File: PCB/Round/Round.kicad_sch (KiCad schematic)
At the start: 59 parts, among them J3 Conn, SW1 ESE13V01D, U1 PN532, U2 QR, Y1 27.12MHz

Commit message: Images
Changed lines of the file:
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@@
 (kicad_sch
-	(version 20231120)
+	(version 20241209)
 	(generator "eeschema")
-	(generator_version "8.0")
+	(generator_version "9.0")
 	(paper "A4")
 	(title_block
@@
 		(comment 1 "www.me.uk")
 	)
+	(text "GND\nVCC\nTX\nRX\nBell"
+		(exclude_from_sim no)
+		(at 241.935 62.865 0)
+		(effects
+			(font
+				(size 1.27 1.27)
+			)
+			(justify left bottom)
+		)
+	)
 	(junction
 		(at 85.09 113.03)
@@
 		)
 	)
-	(text "GND\nVCC\nTX\nRX\nBell"
-		(exclude_from_sim no)
-		(at 241.935 62.865 0)
-		(effects
-			(font
-				(size 1.27 1.27)
-			)
-			(justify left bottom)
-		)
-	)
 	(symbol
 		(lib_id "RevK:PN532-Antenna")
@@
 		)
 	)
+	(embedded_fonts no)
 )

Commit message: PCB Update
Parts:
- D1: LCSC Part # C157737 -> (none); MPN (none) -> C157737
- D10, D4, D5, D6, D7, D8, D9: LCSC Part # C5137770 -> (none); MPN (none) -> C5137770
- D2: LCSC Part # C125108 -> (none); MPN (none) -> C125108
- D3: LCSC Part # C125107 -> (none); MPN (none) -> C125107
- J3: JLCPCB Rotation Offset 90 -> (none); LCSC Part # C780063 -> (none); MPN (none) -> C780063
- L1, L2: LCSC Part # C75639 -> (none); MPN (none) -> C75639
- R4: LCSC Part # C114612 -> (none); MPN (none) -> C114612
- R5: LCSC Part # C22548 -> (none); MPN (none) -> C22548
- U1: JLCPCB Rotation Offset -90 -> (none)
- Y1: JLCPCB Rotation Offset 180 -> (none); LCSC Part # C70591 -> (none); MPN (none) -> C70591
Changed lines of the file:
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@@
 			)
 		)
-		(property "JLCPCB Rotation Offset" "-90"
-			(at 163.83 139.7 0)
-			(effects
-				(font
-					(size 1.27 1.27)
-				)
-				(hide yes)
-			)
-		)
 		(pin "1"
 		)
@@
 			)
 		)
-		(property "LCSC Part #" "C75639"
+		(property "MPN" "C75639"
 			(at 99.06 92.71 90)
 			(effects
@@
 			)
 		)
-		(property "LCSC Part #" "C75639"
+		(property "MPN" "C75639"
 			(at 99.06 113.03 90)
 			(effects
@@
 			)
 		)
-		(property "LCSC Part #" "C70591"
-			(at 158.75 144.78 0)
-			(effects
-				(font
-					(size 1.27 1.27)
-				)
-				(hide yes)
-			)
-		)
-		(property "JLCPCB Rotation Offset" "180"
+		(property "MPN" "C70591"
 			(at 158.75 144.78 0)
 			(effects
@@
 			)
 		)
-		(property "LCSC Part #" "C114612"
+		(property "MPN" "C114612"
 			(at 101.6 127 90)
 			(effects
@@
 			)
 		)
-		(property "LCSC Part #" "C22548"
+		(property "MPN" "C22548"
 			(at 128.27 123.19 0)
 			(effects
@@
 			)
 		)
-		(property "LCSC Part #" "C780063"
-			(at 247.65 57.785 0)
-			(effects
-				(font
-					(size 1.27 1.27)
-				)
-				(hide yes)
-			)
-		)
-		(property "JLCPCB Rotation Offset" "90"
+		(property "MPN" "C780063"
 			(at 247.65 57.785 0)
 			(effects
@@
 			)
 		)
-		(property "LCSC Part #" "C157737"
+		(property "MPN" "C157737"
 			(at 199.39 30.48 0)
 			(effects
@@
 			)
 		)
-		(property "LCSC Part #" "C125108"
+		(property "MPN" "C125108"
 			(at 199.39 45.72 0)
 			(effects
@@
 			)
 		)
-		(property "LCSC Part #" "C125107"
+		(property "MPN" "C125107"
 			(at 199.39 62.23 0)
 			(effects
@@
 			)
 		)
-		(property "LCSC Part #" "C5137770"
+		(property "MPN" "C5137770"
 			(at 257.175 113.03 0)
 			(effects
@@
 			)
 		)
-		(property "LCSC Part #" "C5137770"
+		(property "MPN" "C5137770"
 			(at 257.175 123.19 0)
 			(effects
@@
 			)
 		)
-		(property "LCSC Part #" "C5137770"
+		(property "MPN" "C5137770"
 			(at 257.175 139.7 0)
 			(effects
@@
 			)
 		)
-		(property "LCSC Part #" "C5137770"
+		(property "MPN" "C5137770"
 			(at 199.39 71.12 0)
 			(effects
@@
 			)
 		)
-		(property "LCSC Part #" "C5137770"
+		(property "MPN" "C5137770"
 			(at 267.97 51.435 0)
 			(effects
@@
 			)
 		)
-		(property "LCSC Part #" "C5137770"
+		(property "MPN" "C5137770"
 			(at 199.39 54.61 0)
 			(effects
@@
 			)
 		)
-		(property "LCSC Part #" "C5137770"
+		(property "MPN" "C5137770"
 			(at 199.39 39.37 0)
 			(effects

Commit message: Tidy
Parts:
- removed U2: QR, RevK:QR-PN532, symbol RevK:QR
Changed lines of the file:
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@@
 (kicad_sch
-	(version 20241209)
+	(version 20250114)
 	(generator "eeschema")
 	(generator_version "9.0")
@@
 		(dnp no)
 		(property "Reference" "R4"
-			(at 101.6 132.08 90)
+			(at 101.854 129.54 90)
 			(effects
 				(font
@@
 		)
 		(property "Value" "2k7 1%"
-			(at 101.6 124.0536 90)
+			(at 103.632 127 90)
 			(effects
 				(font
@@
 		(dnp no)
 		(property "Reference" "R6"
-			(at 151.13 31.5722 90)
+			(at 151.13 34.544 90)
 			(effects
 				(font
@@
 		)
 		(property "Value" "10K"
-			(at 151.13 33.8836 90)
+			(at 151.13 36.83 90)
 			(effects
 				(font
@@
 		(dnp no)
 		(property "Reference" "R8"
-			(at 213.36 25.2222 90)
+			(at 213.36 28.448 90)
 			(effects
 				(font
@@
 		)
 		(property "Value" "100R"
-			(at 213.36 27.5336 90)
+			(at 213.36 30.48 90)
 			(effects
 				(font
@@
 		(dnp no)
 		(property "Reference" "R9"
-			(at 213.36 40.4622 90)
+			(at 213.36 43.4086 90)
 			(effects
 				(font
@@
 		)
 		(property "Value" "100R"
-			(at 213.36 42.7736 90)
+			(at 213.36 45.72 90)
 			(effects
 				(font
@@
 		(dnp no)
 		(property "Reference" "R10"
-			(at 213.36 56.9722 90)
+			(at 213.36 59.9186 90)
 			(effects
 				(font
@@
 		)
 		(property "Value" "100R"
-			(at 213.36 59.2836 90)
+			(at 213.36 62.23 90)
 			(effects
 				(font
@@
 		(dnp no)
 		(property "Reference" "R11"
-			(at 228.6 15.0622 90)
+			(at 228.6 18.0086 90)
 			(effects
 				(font
@@
 		)
 		(property "Value" "10K"
-			(at 228.6 17.3736 90)
+			(at 228.6 20.32 90)
 			(effects
 				(font
@@
 		(dnp no)
 		(property "Reference" "R7"
-			(at 158.75 42.0878 90)
+			(at 158.496 39.37 90)
 			(effects
 				(font
@@
 		)
 		(property "Value" "20K"
-			(at 158.75 39.7764 90)
+			(at 158.75 36.83 90)
 			(effects
 				(font
@@
 		(dnp no)
 		(property "Reference" "R15"
-			(at 214.4522 127.635 90)
+			(at 217.3986 127.508 90)
 			(effects
 				(font
@@
 		)
 		(property "Value" "10K"
-			(at 216.7636 127.635 90)
+			(at 219.71 127.508 90)
 			(effects
 				(font
@@
 		(dnp no)
 		(property "Reference" "R14"
-			(at 246.38 124.46 90)
+			(at 246.38 121.92 90)
 			(effects
 				(font
@@
 		)
 		(property "Value" "100R"
-			(at 246.38 121.92 90)
+			(at 246.38 119.38 90)
 			(effects
 				(font
@@
 		(dnp no)
 		(property "Reference" "R13"
-			(at 246.38 111.76 90)
+			(at 246.38 114.3 90)
 			(effects
 				(font
@@
 		)
 		(property "Value" "100R"
-			(at 246.38 114.3 90)
+			(at 246.38 116.84 90)
 			(effects
 				(font
@@
 		(dnp no)
 		(property "Reference" "R12"
-			(at 240.665 140.97 90)
+			(at 240.792 138.43 90)
 			(effects
 				(font
@@
 		)
 		(property "Value" "100R"
-			(at 240.665 138.43 90)
+			(at 240.792 135.89 90)
 			(effects
 				(font
@@
 					(unit 1)
 				)
-			)
-		)
-	)
-	(symbol
-		(lib_name "QR_1")
-		(lib_id "RevK:QR")
-		(at 273.05 173.355 0)
-		(unit 1)
-		(exclude_from_sim no)
-		(in_bom no)
-		(on_board yes)
-		(dnp no)
-		(property "Reference" "U2"
-			(at 273.05 174.625 0)
-			(effects
-				(font
-					(size 1.27 1.27)
-				)
-				(hide yes)
-			)
-		)
-		(property "Value" "QR"
-			(at 273.05 174.625 0)
-			(effects
-				(font
-					(size 1.27 1.27)
-				)
-				(hide yes)
-			)
-		)
-		(property "Footprint" "RevK:QR-PN532"
-			(at 273.05 173.355 0)
-			(effects
-				(font
-					(size 1.27 1.27)
-				)
-				(hide yes)
-			)
-		)
-		(property "Datasheet" ""
-			(at 273.05 173.355 0)
-			(effects
-				(font
-					(size 1.27 1.27)
-				)
-				(hide yes)
-			)
-		)
-		(property "Description" ""
-			(at 273.05 173.355 0)
-			(effects
-				(font
-					(size 1.27 1.27)
-				)
-				(hide yes)
-			)
-		)
-		(property "Note" "Non part, PCB printed"
-			(at 273.05 173.355 0)
-			(effects
-				(font
-					(size 1.27 1.27)
-				)
-				(hide yes)
-			)
-		)
-		(instances
-			(project "Round"
-				(path "/0217dfc4-fc13-4699-99ad-d9948522648e"
-					(reference "U2")
-					(unit 1)
-				)

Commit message: Tweaks
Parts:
- R1, R3: MPN (none) -> 0603; Part No 0603-0R -> (none)
- R10, R13, R14, R8, R9: MPN (none) -> C22775; Part No 0603-100R -> (none)
- R11, R15, R6: MPN (none) -> C25804; Part No 0603-10K -> (none)
- R12: MPN (none) -> 0603-100R; Part No 0603-100R -> (none)
- R2: MPN (none) -> C17477; Part No 0805-0R -> (none)
- R4: Manufacturer YAGEO -> (none); Note 0603 -> (none); Part No RC0603FR-102K7L -> (none)
- R7: MPN (none) -> C4184; Manufacturer YAGEO -> (none); Note 0603 -> (none); Part No RC0603JR-1020KL -> (none)
- U1: MPN (none) -> C28925; Manufacturer NXP Semiconductors -> (none); Part No PN5321A3HN/C106,51 -> (none)

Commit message: Change part
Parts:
- J3: MPN C780063 -> C2883802; Manufacturer Samtec -> (none); PartNo TSM-105-02-L-SV -> (none)
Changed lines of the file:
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@@
 			)
 		)
-		(property "Note" ""
+		(property "MPN" "C2883802"
 			(at 247.65 57.785 0)
 			(effects
-				(font
-					(size 1.27 1.27)
-				)
-				(hide yes)
-			)
-		)
-		(property "PartNo" "TSM-105-02-L-SV"
-			(at 247.65 57.785 0)
-			(effects
-				(font
-					(size 1.27 1.27)
-				)
-				(hide yes)
-			)
-		)
-		(property "Manufacturer" "Samtec"
-			(at 247.65 57.785 0)
-			(effects
-				(font
-					(size 1.27 1.27)
-				)
-				(hide yes)
-			)
-		)
-		(property "MPN" "C780063"
-			(at 247.65 57.785 0)
-			(effects

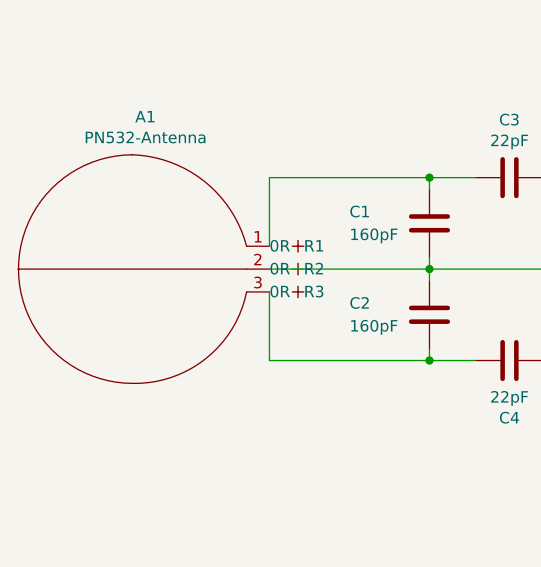
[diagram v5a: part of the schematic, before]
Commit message: Updated case logic from PCB
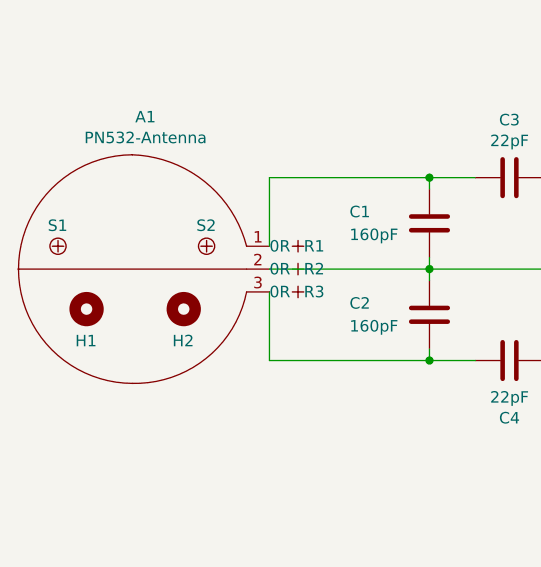
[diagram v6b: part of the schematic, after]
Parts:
- added H1, H2: MountingHole, RevK:MountingHole_4mm, symbol Mechanical:MountingHole
- added S1, S2: Screw, RevK:Screw, symbol RevK:Screw

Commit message: Not sure
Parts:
- J3: Rotation Offset (none) -> 90
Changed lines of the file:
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@@
+			)
+		)
+		(property "Rotation Offset" "90"
+			(at 247.65 57.785 0)
+			(effects
+				(font
+					(size 1.27 1.27)
+				)
+				(hide yes)
 			)
 		)
